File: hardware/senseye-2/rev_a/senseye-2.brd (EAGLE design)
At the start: 149.8 x 55.3 mm, 19 parts, among them U1 ADC121S101, U2 ADC121S101, U3 ADC121S101

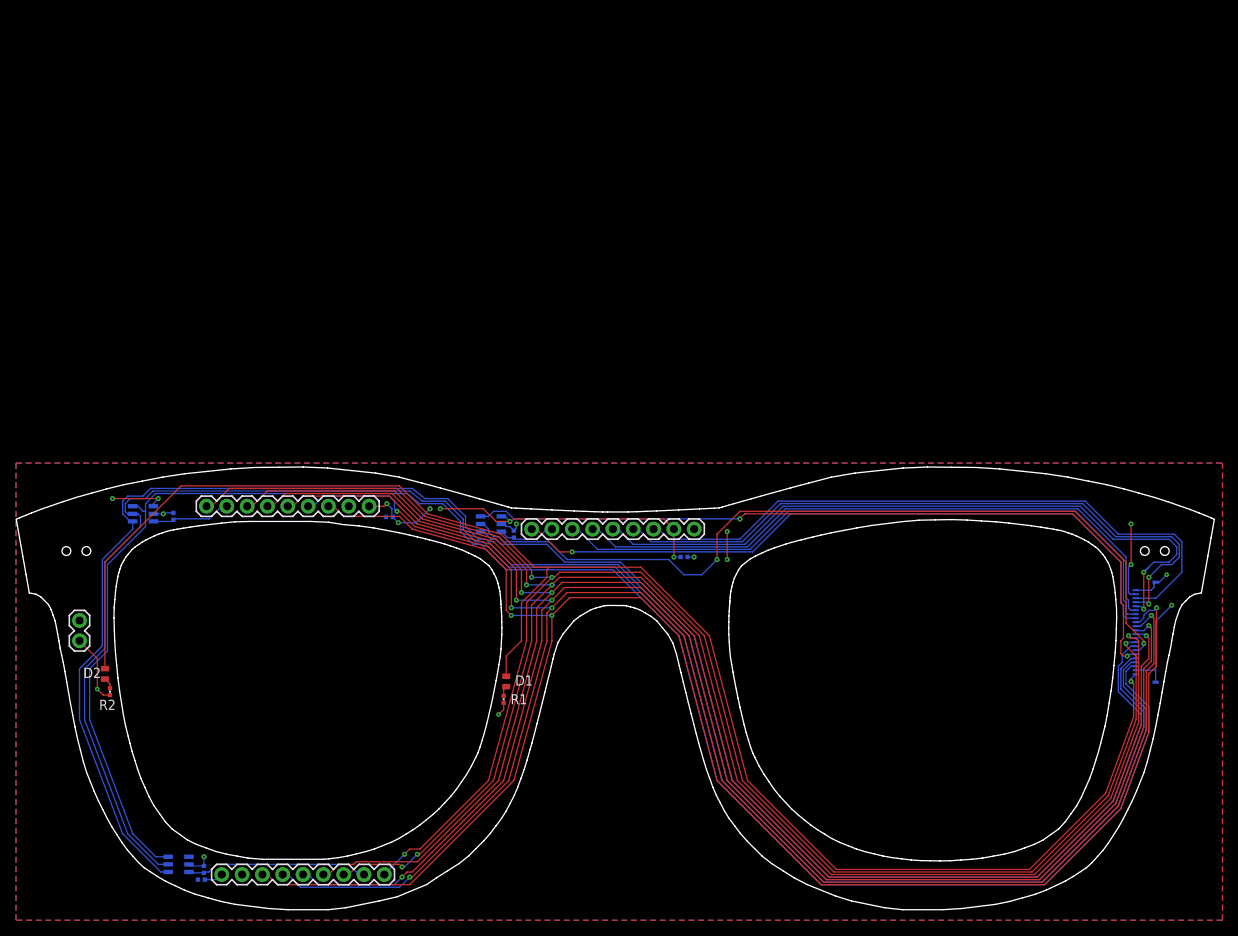
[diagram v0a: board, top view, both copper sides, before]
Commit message: moved all to 0,0 origin
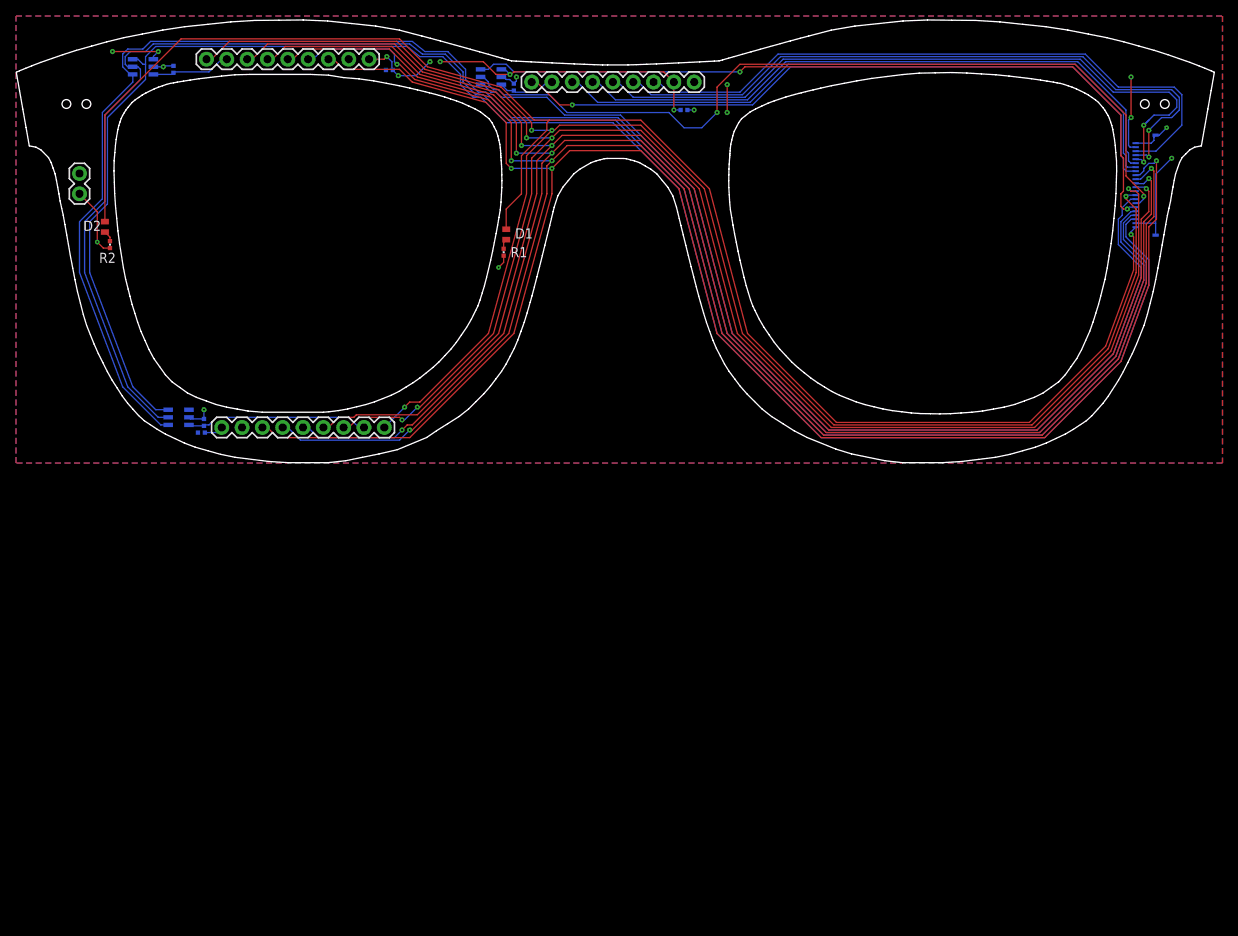
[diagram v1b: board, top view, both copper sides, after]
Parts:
- moved C1 55.9 mm to (83.5, 44.1)
- moved C2 55.9 mm to (23.2, 3.81)
- moved C3 55.9 mm to (46.7, 49.1)
- moved JP1 55.9 mm to (64.5, 47.6)
- moved JP2 55.9 mm to (46.0, 4.45)
- moved JP3 55.9 mm to (23.8, 50.5)
- moved JP4 55.9 mm to (7.94, 33.7)
- moved R3 55.9 mm to (62.2, 47.0)
- moved U$1 55.9 mm to (78.7, 41.0)
- moved U3 55.9 mm to (15.9, 49.5)
- moved D1 55.9 mm to (61.3, 28.6)
- moved D2 55.9 mm to (11.1, 29.5)
- moved JP5 55.9 mm to (140.0, 34.7)
- moved R1 55.9 mm to (61.0, 26.4)
- moved R2 55.9 mm to (11.7, 27.3)
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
